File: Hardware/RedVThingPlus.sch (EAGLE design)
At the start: 96 parts, among them J1 FEMALE 2x3, J2 USB Female Type C Connector, J5 JTAG, Q1 3.1A/30V/105mΩ, U1 MCP73831, U2 1.8V, U3 AP2112-3.3V, U4 FE310, U5 32MB, Y1 32.768KHZ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

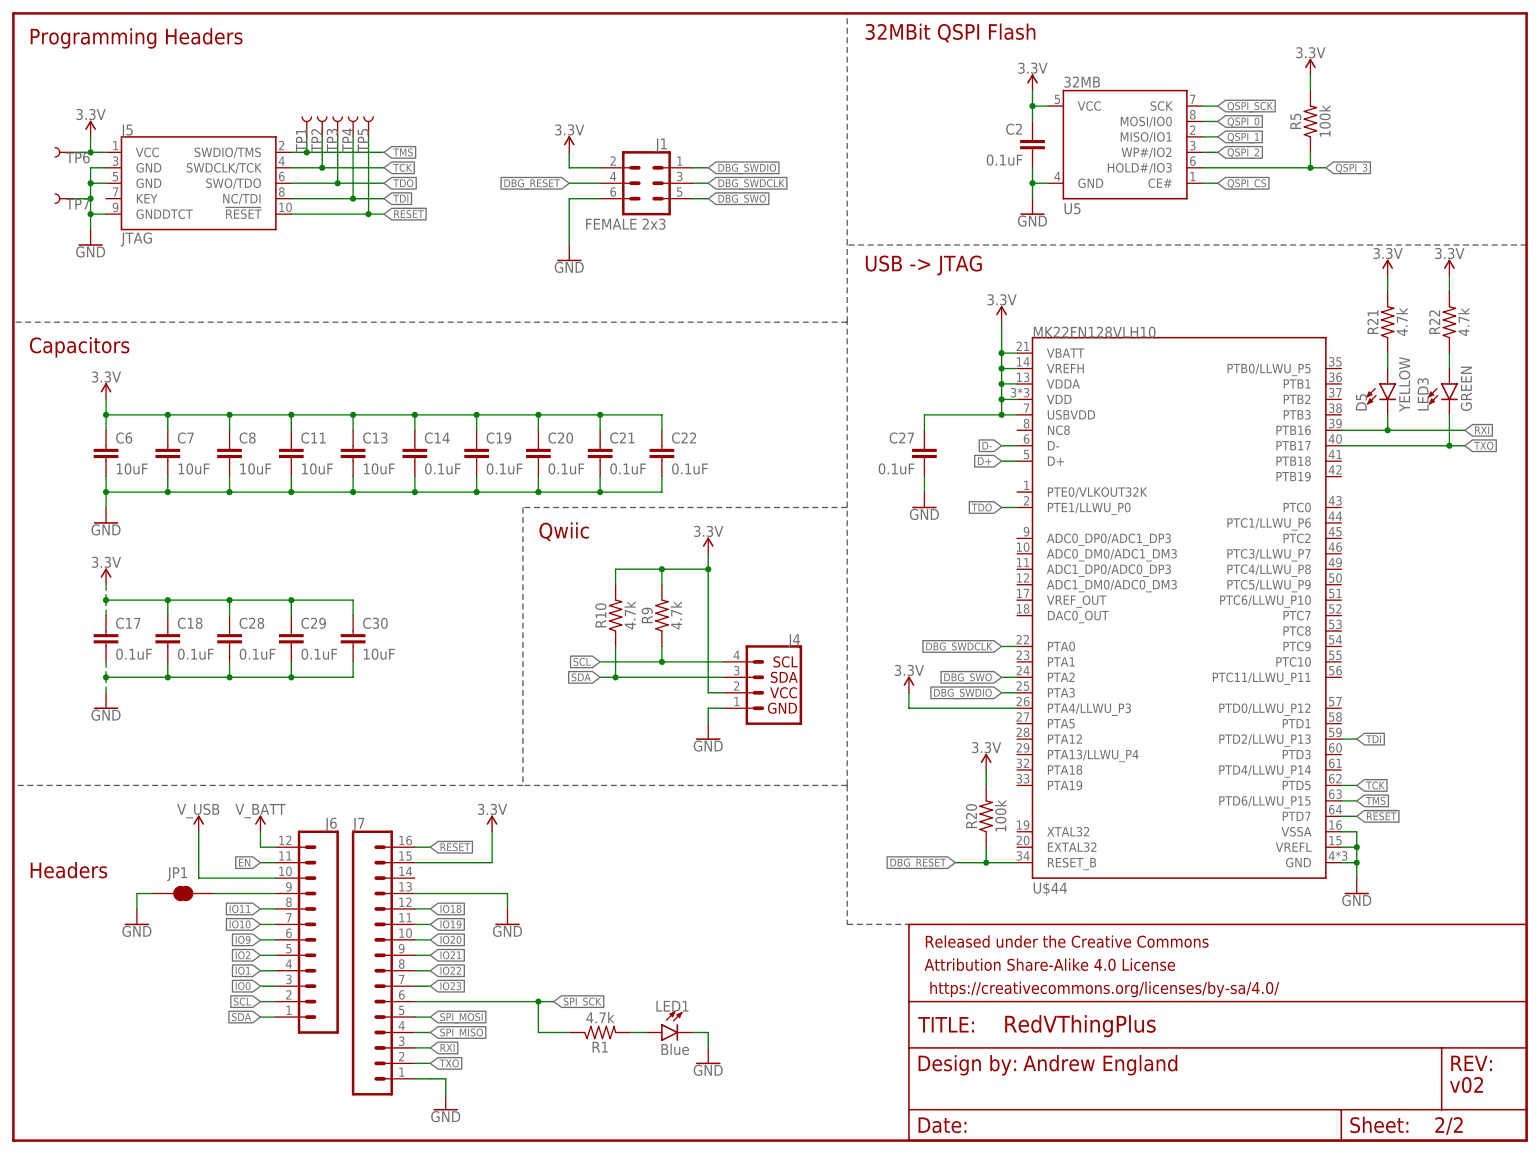
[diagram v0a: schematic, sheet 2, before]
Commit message: all components placed, midway through routing
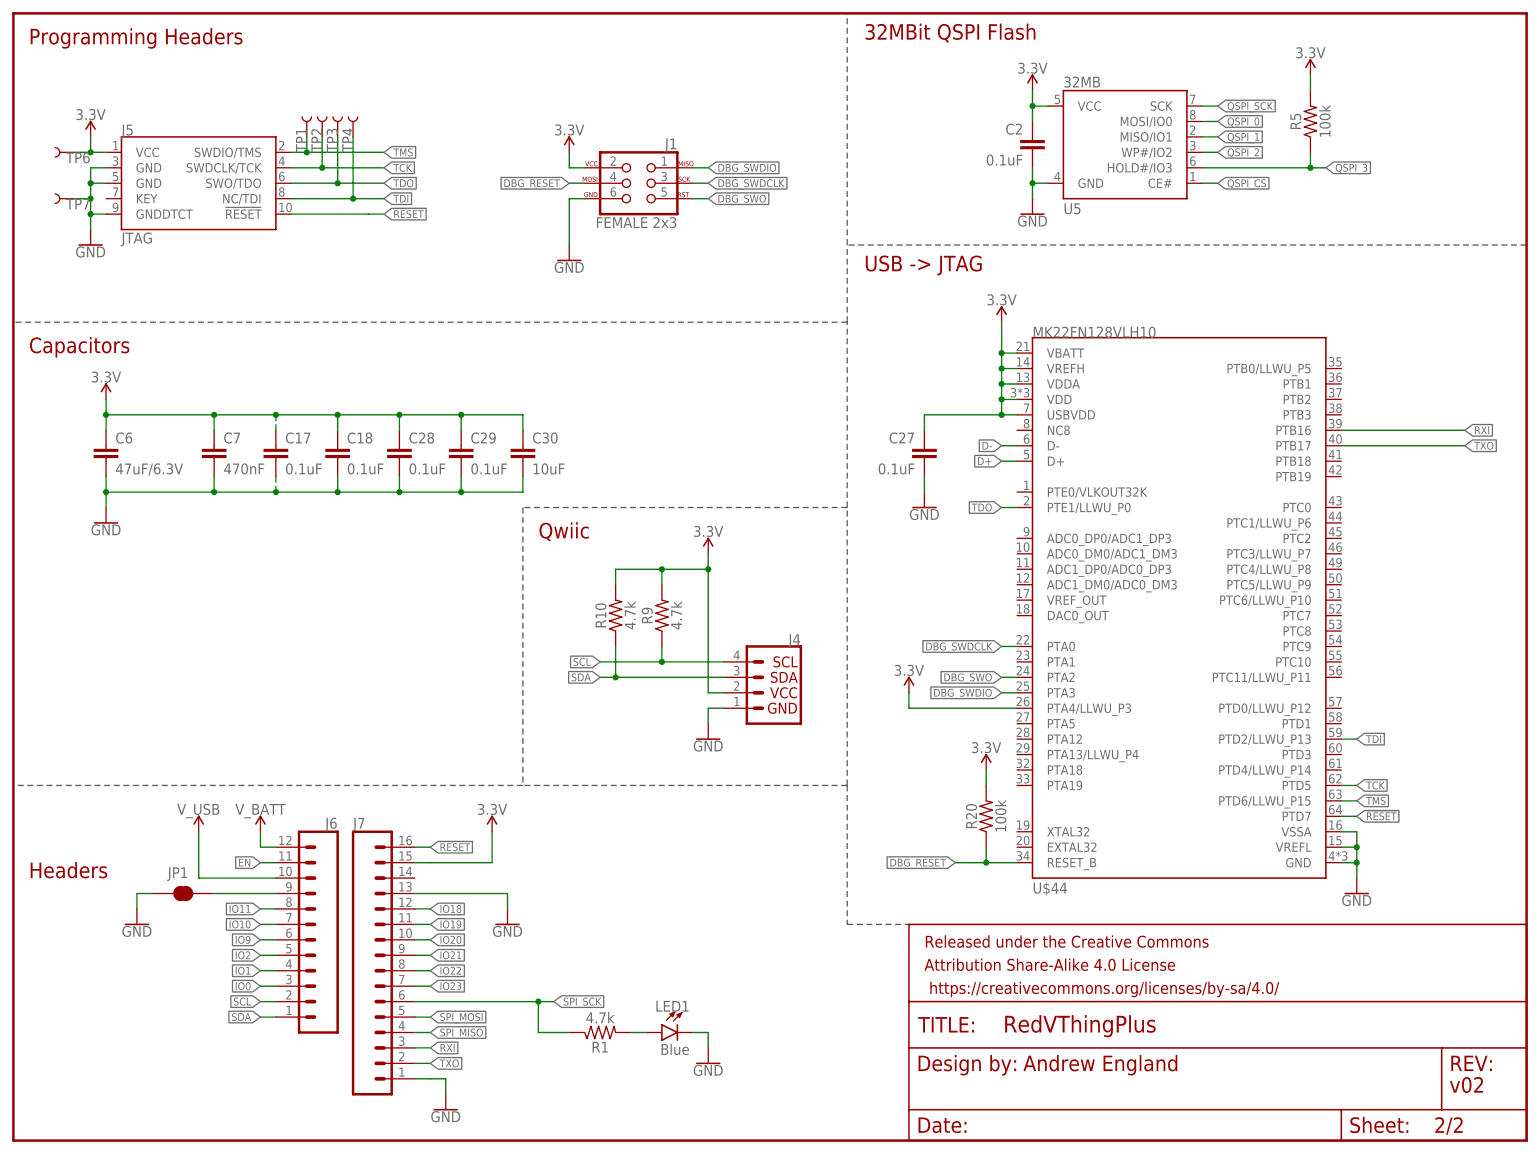
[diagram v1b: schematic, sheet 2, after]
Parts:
- removed C11, C13, C8: 10uF, SparkFun-Capacitors:10UF-0603-6.3V-20%
- removed C14, C19, C20, C21, C22: 0.1uF, SparkFun-Capacitors:0.1UF-0603-25V-(+80/-20%)
- removed D5: YELLOW, SparkFun-LED:LED-YELLOW_HIDDENSILK
- removed LED3: GREEN, SparkFun-LED:LED-GREENLILYPAD
- removed R21, R22: 4.7k, SparkFun-Resistors:4.7KOHM-0603-1/10W-1%
- removed TP5: TEST-POINT3, SparkFun-Connectors:TEST-POINT3
- C6: value 10uF -> 47uF/6.3V; device SparkFun-Capacitors:10UF-0603-6.3V-20% -> SparkFun-Capacitors:47UF
- C7: value 10uF -> 470nF; device SparkFun-Capacitors:10UF-0603-6.3V-20% -> SparkFun-Capacitors:470NF-0603-10V-10%-X5R
- J1: device SparkFun-Connectors:CONN_03X2FEMALE -> SparkFun-Connectors:AVR_SPI_PROG_3X2TESTPOINTS
- J6: device SparkFun-Connectors:CONN_12 -> SparkFun-Connectors:CONN_12SM_SQ_NO_SILK
- J7: device SparkFun-Connectors:CONN_16 -> SparkFun-Connectors:CONN_161X16_SM_SQ_NOSILK
- S1, S2: value MOMENTARY-SWITCH-SPST-SMD-6.2MM-TALL -> MOMENTARY-SWITCH-SPST-SMD-4.6X2.8MM; device SparkFun-Switches:MOMENTARY-SWITCH-SPST-SMD-6.2MM-TALL -> SparkFun-Switches:MOMENTARY-SWITCH-SPST-SMD-4.6X2.8MM
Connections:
- removed net N$13: D5.A, R21.1
- removed net N$6: LED3.A, R22.1
- net !RESET: no longer TP5.1
- net 3.3V: no longer C11.1, C13.1, C14.1, C19.1, C20.1, C21.1, C22.1, C8.1, R21.2, R22.2
- net GND: no longer C11.2, C13.2, C14.2, C19.2, C20.2, C21.2, C22.2, C8.2
- net RXI: no longer D5.C
- net TXO: no longer LED3.C
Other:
- moved on the sheet: C17, C18, C28, C29, C30, C7

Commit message: initial layout complete, needs silk
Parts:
- removed J5: JTAG, SparkFun-Connectors:CORTEX_JTAG_DEBUG_SMD
- removed TP1, TP2, TP3, TP4, TP6, TP7: TEST-POINT3, SparkFun-Connectors:TEST-POINT3
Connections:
- net !RESET: no longer J5.!RESET
- net 3.3V: no longer J5.VCC, TP6.1
- net GND: no longer J5.GND@3, J5.GND@5, J5.GNDDTCT, TP7.1
- net TCK: no longer J5.SWDCLK/TCK, TP2.1
- net TDI: no longer J5.NC/TDI, TP4.1
- net TDO: no longer J5.SWO/TDO, TP3.1
- net TMS: no longer J5.SWDIO/TMS, TP1.1
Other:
- note added: "Programming Headers & Test Points"
- note removed: "Programming Headers"
- moved on the sheet: J1

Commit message: v10 changes for Reds design review
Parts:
- removed JP1: JUMPER-SMT_2_NC_TRACE_SILK, SparkFun-Jumpers:JUMPER-SMT_2_NC_TRACE_SILK
- removed JP3, JP4, JP5, JP6: STAND-OFF, SparkFun:STAND-OFF
- removed U$44: MK22FN128VLH10, SparkFun-IC-Comms:MK22FN128VLH10
- added I2C: JUMPER-SMT_3_NO_NO-SILK, SparkFun-Jumpers:JUMPER-SMT_3_NO_NO-SILK
- added NC/GND: JUMPER-SMT_2_NO_NO-SILK, SparkFun-Jumpers:JUMPER-SMT_2_NO_NO-SILK
- added U6: FE310, SparkFun-IC-Microcontroller:SIFIVE_FE310
- J4: value (none) -> QWIIC_RIGHT_ANGLE
- U2: value 1.8V -> AP2127K-1.8V
- U4: value FE310 -> MK22FN128VLH10; device SparkFun-IC-Microcontroller:SIFIVE_FE310 -> SparkFun-IC-Comms:MK22FN128VLH10
- U5: value 32MB -> 32MBit
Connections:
- new net N$5: I2C.1, R9.2
- new net N$6: I2C.3, R10.2
- net !RESET: now also U4.PTD7, U6.AON_ERST_N; no longer U$44.PTD7, U4.AON_ERST_N
- net !WAKE: now also U6.AON_DWAKEUP_N; no longer U4.AON_DWAKEUP_N
- net 1.8V: now also U6.VDD_CORE; no longer U4.VDD_CORE
- net 3.3V: now also I2C.2, U4.PTA4/LLWU_P3, U4.USBVDD, U4.VBATT, U4.VDD, U4.VDDA, U4.VREFH, U6.AON_VDD, U6.AON_VDD_IO, U6.OTP_AIVDD, U6.VDD_IO; no longer R10.2, R9.2, U$44.PTA4/LLWU_P3, U$44.USBVDD, U$44.VBATT, U$44.VDD, U$44.VDDA, U$44.VREFH, U4.AON_VDD, U4.AON_VDD_IO, U4.OTP_AIVDD, U4.VDD_IO
- net CORE_ENABLE: now also U6.AON_PMU_OUT_0; no longer U4.AON_PMU_OUT_0
- net D+: now also U4.D+; no longer U$44.D+
- net D-: now also U4.D-; no longer U$44.D-
- net DBG_RESET: now also U4.RESET_B; no longer U$44.RESET_B
- net DBG_SWDCLK: now also U4.PTA0; no longer U$44.PTA0
- net DBG_SWDIO: now also U4.PTA3; no longer U$44.PTA3
- net DBG_SWO: now also U4.PTA2; no longer U$44.PTA2
- net GND: now also NC/GND.1, U4.VREFL, U4.VSSA, U6.AON_PSD_LFCLKSEL, U6.GND; no longer J2.SHLD, JP1.1, U$44.GND, U$44.VREFL, U$44.VSSA, U4.AON_PSD_LFCLKSEL
- net IO0: now also U6.IO0; no longer U4.IO0
- net IO1: now also U6.IO1; no longer U4.IO1
- net IO10: now also U6.IO10; no longer U4.IO10
- net IO11: now also U6.IO11; no longer U4.IO11
- net IO18: now also U6.IO18; no longer U4.IO18
- net IO19: now also U6.IO19; no longer U4.IO19
- net IO2: now also U6.IO2; no longer U4.IO2
- net IO20: now also U6.IO20; no longer U4.IO20
- net IO21: now also U6.IO21; no longer U4.IO21
- net IO22: now also U6.IO22; no longer U4.IO22
- net IO23: now also U6.IO23; no longer U4.IO23
- net IO9: now also U6.IO9; no longer U4.IO9
- net N$10: now also U6.PLL_AVSS; no longer U4.PLL_AVSS
- net N$3: now also U6.XTAL_OUT; no longer U4.XTAL_OUT
- net N$4: now also NC/GND.2; no longer JP1.2
- net N$7: now also U6.XTAL_IN; no longer U4.XTAL_IN
- net N$8: now also U6.AON_PSD_LFALTCLK; no longer U4.AON_PSD_LFALTCLK
- net PLL_AVDD: now also U6.PLL_AVDD; no longer U4.PLL_AVDD
- net QSPI_0: now also U6.QSPI_DQ_0; no longer U4.QSPI_DQ_0
- net QSPI_1: now also U6.QSPI_DQ_1; no longer U4.QSPI_DQ_1
- net QSPI_2: now also U6.QSPI_DQ_2; no longer U4.QSPI_DQ_2
- net QSPI_3: now also U6.QSPI_DQ_3; no longer U4.QSPI_DQ_3
- net QSPI_CS: now also U6.QSPI_CS; no longer U4.QSPI_CS
- net QSPI_SCK: now also U6.QSPI_SCK; no longer U4.QSPI_SCK
- net RXI: now also U4.PTB17, U6.IO16; no longer U$44.PTB16, U4.IO16
- net SCL: now also U6.IO13; no longer U4.IO13
- net SDA: now also U6.IO12; no longer U4.IO12
- net SPI_MISO: now also U6.IO4; no longer U4.IO4
- net SPI_MOSI: now also U6.IO3; no longer U4.IO3
- net SPI_SCK: now also U6.IO5; no longer U4.IO5
- net TCK: now also U4.PTD5, U6.JTAG_TCK; no longer U$44.PTD5, U4.JTAG_TCK
- net TDI: now also U4.PTD2/LLWU_P13, U6.JTAG_TDI; no longer U$44.PTD2/LLWU_P13, U4.JTAG_TDI
- net TDO: now also U4.PTE1/LLWU_P0, U6.JTAG_TDO; no longer U$44.PTE1/LLWU_P0, U4.JTAG_TDO
- net TMS: now also U4.PTD6/LLWU_P15, U6.JTAG_TMS; no longer U$44.PTD6/LLWU_P15, U4.JTAG_TMS
- net TXO: now also U4.PTB16, U6.IO17; no longer U$44.PTB17, U4.IO17
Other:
- note added: "Close the I2C jumper if your slave doesn't have it's own pullups."
- note added: "Close the NC/GND jumper to connect the NC pad to GND"
- note added: "VIN: 2.5-6.0V"
- note added: "v10"
- note removed: "Based on Arduino by: M.Banzi, D.Cuartielles, T.Igoe, G.Martino, D.Mellis"
- note removed: "v02"
- moved on the sheet: J4, R10, R9

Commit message: post review changes
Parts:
- added LOGO2: SFE_LOGO_FLAME.2_INCH, SparkFun-Aesthetics:SFE_LOGO_FLAME.2_INCH
- LED1: value Blue -> BLUE; device SparkFun-LED:LED-BLUE_HIDDENSILK -> SparkFun-LED:LED-BLUE0603; PROD_ID DIO-09911 -> (none)
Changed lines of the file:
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@@
 <part name="C15" library="SparkFun-Capacitors" deviceset="10UF-POLAR" device="-EIA3216-16V-10%(TANT)" value="10uF"/>
 <part name="LED2" library="SparkFun-LED" deviceset="LED-RED" device="1206" value="RED"/>
-<part name="LED1" library="SparkFun-LED" deviceset="LED-BLUE" device="_HIDDENSILK" value="Blue">
-<attribute name="PROD_ID" value="DIO-09911"/>
-</part>
+<part name="LED1" library="SparkFun-LED" deviceset="LED-BLUE" device="0603" value="BLUE"/>
 <part name="F1" library="SparkFun-Fuses" deviceset="PPTC" device="_6V500MA" value="6V 0.5A"/>
 <part name="GND28" library="SparkFun-PowerSymbols" deviceset="GND" device=""/>
@@
 <part name="LOGO1" library="SparkFun-Aesthetics" deviceset="SFE_LOGO_NAME_FLAME" device=".1_INCH"/>
 <part name="I2C" library="SparkFun-Jumpers" deviceset="JUMPER-SMT_3_NO" device="_NO-SILK"/>
+<part name="LOGO2" library="SparkFun-Aesthetics" deviceset="SFE_LOGO_FLAME" device=".2_INCH" value="SFE_LOGO_FLAME.2_INCH"/>
 </parts>
 <sheets>
@@
 <attribute name="NAME" x="102.108" y="85.217" size="1.778" layer="95" font="vector"/>
 </instance>
+<instance part="LOGO2" gate="G$1" x="134.62" y="2.54"/>
 </instances>
 <busses>

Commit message: post qc double check changes
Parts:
- removed LED2: RED, SparkFun-LED:LED-RED1206
- removed R2: 10k, SparkFun-Resistors:10KOHM-0603-1/10W-1%
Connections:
- removed net N$2: LED2.A, R2.1
- net 5V: no longer R2.2
- net GND: no longer LED2.C
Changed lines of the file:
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@@
 <part name="R1" library="SparkFun-Resistors" deviceset="4.7KOHM" device="-0603-1/10W-1%" value="4.7k"/>
 <part name="GND3" library="SparkFun-PowerSymbols" deviceset="GND" device=""/>
-<part name="R2" library="SparkFun-Resistors" deviceset="10KOHM" device="-0603-1/10W-1%" value="10k"/>
-<part name="GND4" library="SparkFun-PowerSymbols" deviceset="GND" device=""/>
 <part name="C10" library="SparkFun-Capacitors" deviceset="0.1UF" device="-0603-25V-(+80/-20%)" value="0.1uF"/>
 <part name="JP8" library="SparkFun" deviceset="FIDUCIAL" device="1X2"/>
@@
 <part name="C12" library="SparkFun-Capacitors" deviceset="0.1UF" device="-0603-25V-(+80/-20%)" value="0.1uF"/>
 <part name="C15" library="SparkFun-Capacitors" deviceset="10UF-POLAR" device="-EIA3216-16V-10%(TANT)" value="10uF"/>
-<part name="LED2" library="SparkFun-LED" deviceset="LED-RED" device="1206" value="RED"/>
 <part name="LED1" library="SparkFun-LED" deviceset="LED-BLUE" device="0603" value="BLUE"/>
 <part name="F1" library="SparkFun-Fuses" deviceset="PPTC" device="_6V500MA" value="6V 0.5A"/>
@@
 <part name="GND7" library="SparkFun-PowerSymbols" deviceset="GND" device=""/>
 <part name="FRAME1" library="SparkFun-Aesthetics" deviceset="FRAME-LETTER" device=""/>
-<part name="U$13" library="SparkFun-PowerSymbols" deviceset="5V" device=""/>
 <part name="S1" library="SparkFun-Switches" deviceset="MOMENTARY-SWITCH-SPST" device="-SMD-4.6X2.8MM" value="MOMENTARY-SWITCH-SPST-SMD-4.6X2.8MM"/>
 <part name="S2" library="SparkFun-Switches" deviceset="MOMENTARY-SWITCH-SPST" device="-SMD-4.6X2.8MM" value="MOMENTARY-SWITCH-SPST-SMD-4.6X2.8MM"/>
@@
 </plain>
 <instances>
-<instance part="R2" gate="G$1" x="162.56" y="121.92" smashed="yes" rot="R90">
-<attribute name="NAME" x="161.036" y="121.92" size="1.778" layer="95" font="vector" rot="R90" align="bottom-center"/>
-<attribute name="VALUE" x="164.084" y="121.92" size="1.778" layer="96" font="vector" rot="R90" align="top-center"/>
-</instance>
-<instance part="GND4" gate="1" x="162.56" y="101.6" smashed="yes">
-<attribute name="VALUE" x="162.56" y="101.346" size="1.778" layer="96" align="top-center"/>
-</instance>
 <instance part="C10" gate="G$1" x="68.58" y="33.02" smashed="yes" rot="MR0">
 <attribute name="NAME" x="74.676" y="35.941" size="1.778" layer="95" font="vector" rot="MR0"/>
@@
 <attribute name="NAME" x="98.044" y="36.195" size="1.778" layer="95" font="vector" rot="MR0"/>
 <attribute name="VALUE" x="98.044" y="31.369" size="1.778" layer="96" font="vector" rot="MR0"/>
-</instance>
-<instance part="LED2" gate="G$1" x="162.56" y="111.76" smashed="yes">
-<attribute name="PROD_ID" x="162.56" y="111.76" size="1.778" layer="96" display="off"/>
-<attribute name="NAME" x="159.131" y="107.188" size="1.778" layer="95" font="vector" rot="R90"/>
-<attribute name="VALUE" x="164.465" y="107.188" size="1.778" layer="96" font="vector" rot="R90" align="top-left"/>
 </instance>
 <instance part="F1" gate="F1" x="76.2" y="48.26" smashed="yes">
@@
 <instance part="GND7" gate="1" x="15.24" y="91.44" smashed="yes">
 <attribute name="VALUE" x="15.24" y="91.186" size="1.778" layer="96" align="top-center"/>
-</instance>
-<instance part="U$13" gate="G$1" x="162.56" y="129.54" smashed="yes">
-<attribute name="VALUE" x="162.56" y="132.334" size="1.778" layer="96" align="bottom-center"/>
 </instance>
 <instance part="S1" gate="G$1" x="109.22" y="93.98" smashed="yes" rot="MR270">
@@
 <pinref part="U2" gate="G$1" pin="IN"/>
 <wire x1="195.58" y1="127" x2="193.04" y2="127" width="0.1524" layer="91"/>
-</segment>
-<segment>
-<wire x1="162.56" y1="129.54" x2="162.56" y2="127" width="0.1524" layer="91"/>
-<pinref part="R2" gate="G$1" pin="2"/>
-<pinref part="U$13" gate="G$1" pin="5V"/>
 </segment>
 <segment>
@@
 <net name="GND" class="0">
 <segment>
-<wire x1="162.56" y1="104.14" x2="162.56" y2="106.68" width="0.1524" layer="91"/>
-<pinref part="GND4" gate="1" pin="GND"/>
-<pinref part="LED2" gate="G$1" pin="C"/>
-</segment>
-<segment>
 <pinref part="C16" gate="G$1" pin="2"/>
 <pinref part="GND28" gate="1" pin="GND"/>
@@
 </segment>
 </net>
-<net name="N$2" class="0">
-<segment>
-<wire x1="162.56" y1="116.84" x2="162.56" y2="114.3" width="0.1524" layer="91"/>
-<pinref part="R2" gate="G$1" pin="1"/>
-<pinref part="LED2" gate="G$1" pin="A"/>
-</segment>
-</net>

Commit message: updating to final silk
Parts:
- removed LOGO1: SFE_LOGO_NAME_FLAME.1_INCH, SparkFun-Aesthetics:SFE_LOGO_NAME_FLAME.1_INCH
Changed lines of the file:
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@@
 <part name="U6" library="SparkFun-IC-Microcontroller" deviceset="SIFIVE_FE310" device="" value="FE310"/>
 <part name="U4" library="SparkFun-IC-Comms" deviceset="MK22FN128VLH10" device="" value="MK22FN128VLH10"/>
-<part name="LOGO1" library="SparkFun-Aesthetics" deviceset="SFE_LOGO_NAME_FLAME" device=".1_INCH"/>
 <part name="I2C" library="SparkFun-Jumpers" deviceset="JUMPER-SMT_3_NO" device="_NO-SILK"/>
 <part name="LOGO2" library="SparkFun-Aesthetics" deviceset="SFE_LOGO_FLAME" device=".2_INCH" value="SFE_LOGO_FLAME.2_INCH"/>
@@
 <instance part="SUPPLY27" gate="G$1" x="218.44" y="76.2"/>
 <instance part="U6" gate="G$1" x="43.18" y="132.08"/>
-<instance part="LOGO1" gate="G$1" x="88.9" y="2.54"/>
 </instances>
 <busses>

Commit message: updating to 100 Ohm resistor on R8
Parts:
- R8: value 100k -> 100; device SparkFun-Resistors:100KOHM-0603-1/10W-1% -> SparkFun-Resistors:100OHM-0603-1/10W-1%
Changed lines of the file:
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@@
 <part name="C25" library="SparkFun-Capacitors" deviceset="0.1UF" device="-0603-25V-(+80/-20%)" value="0.1uF"/>
 <part name="C26" library="SparkFun-Capacitors" deviceset="0.1UF" device="-0603-25V-(+80/-20%)" value="0.1uF"/>
-<part name="R8" library="SparkFun-Resistors" deviceset="100KOHM" device="-0603-1/10W-1%" value="100k"/>
+<part name="R8" library="SparkFun-Resistors" deviceset="100OHM" device="-0603-1/10W-1%" value="100"/>
 <part name="R9" library="SparkFun-Resistors" deviceset="4.7KOHM" device="-0603-1/10W-1%" value="4.7k"/>
 <part name="R10" library="SparkFun-Resistors" deviceset="4.7KOHM" device="-0603-1/10W-1%" value="4.7k"/>
